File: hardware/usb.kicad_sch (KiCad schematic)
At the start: 24 parts, among them J3 USB_C_Receptacle, Q1 Q_NMOS_DGS, Q2 MBT2222ADW1T1, U10 CP2102N-Axx-xQFN24

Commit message: fixing submodule
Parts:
- removed Q1: Q_NMOS_DGS, Package_TO_SOT_SMD:SOT-323_SC-70, symbol Device:Q_NMOS_DGS
- removed R27, R60: 100k, Resistor_SMD:R_0402_1005Metric, symbol Device:R_Small
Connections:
- net CP2102N_~{SUS}: now reaches R29.1, U10.15 (~{SUSPEND})
- net CP2102N_RTS: now reaches Q2.4 (E2), R30.2, U10.19 (~{RTS})
- net CP2102N_DTR: now reaches Q2.1 (E1), R31.1, U10.23 (~{DTR})
- net USB_POWER_GOOD: now reaches U10.8 (VBUS)
- net DTR_BASE: now reaches Q2.5 (B2), R31.2
- net ~{RTS}_BASE: now reaches Q2.2 (B1), R30.1
- net 3V3_CORE renamed VDD_USB_3V3
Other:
- moved on the sheet: Q2A, Q2B, R30, R31

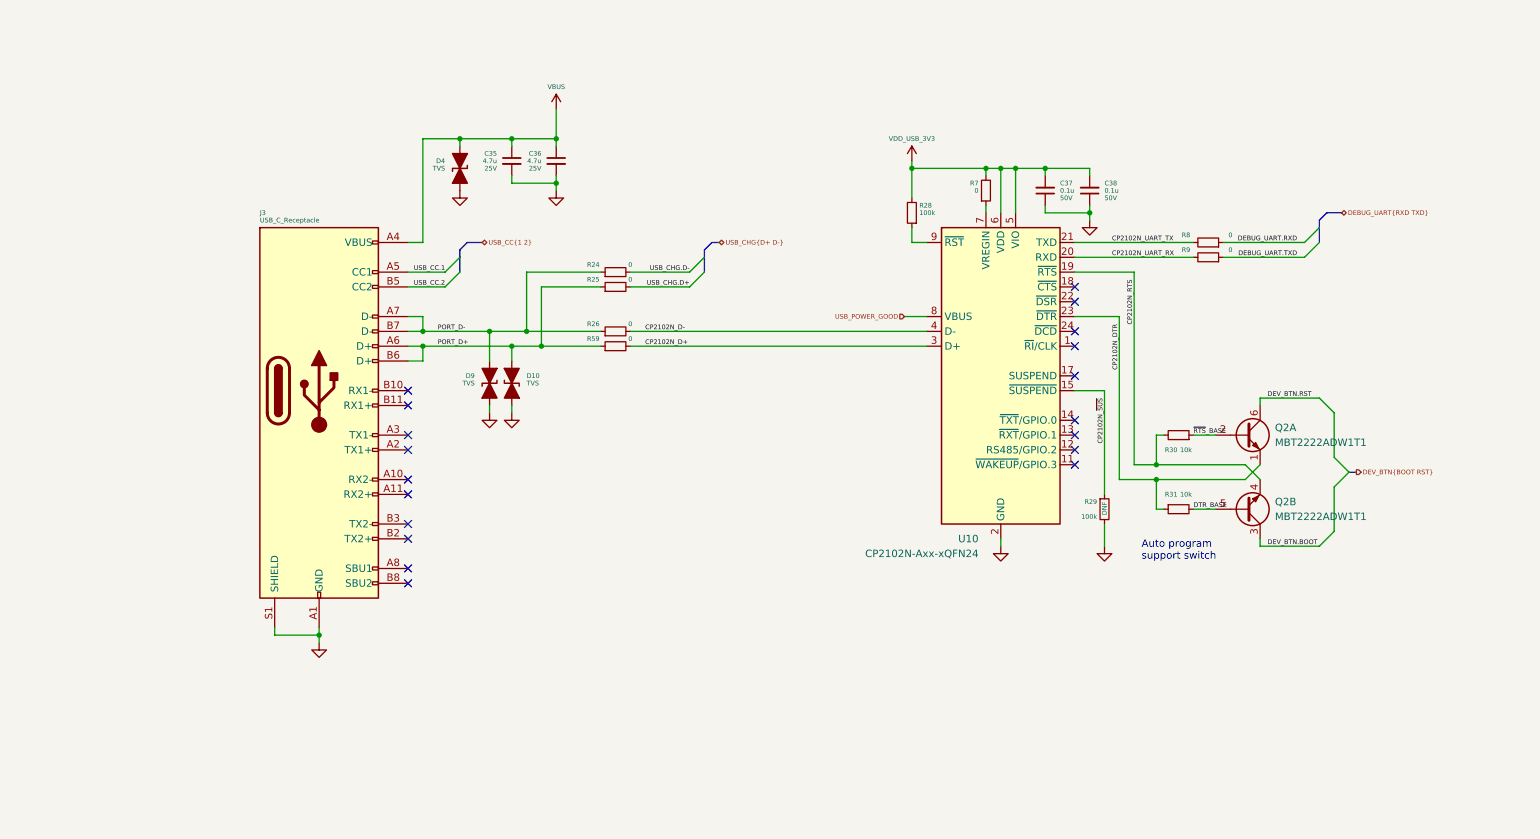
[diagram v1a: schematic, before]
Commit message: schematic tidy up, component placement, shielding investigation
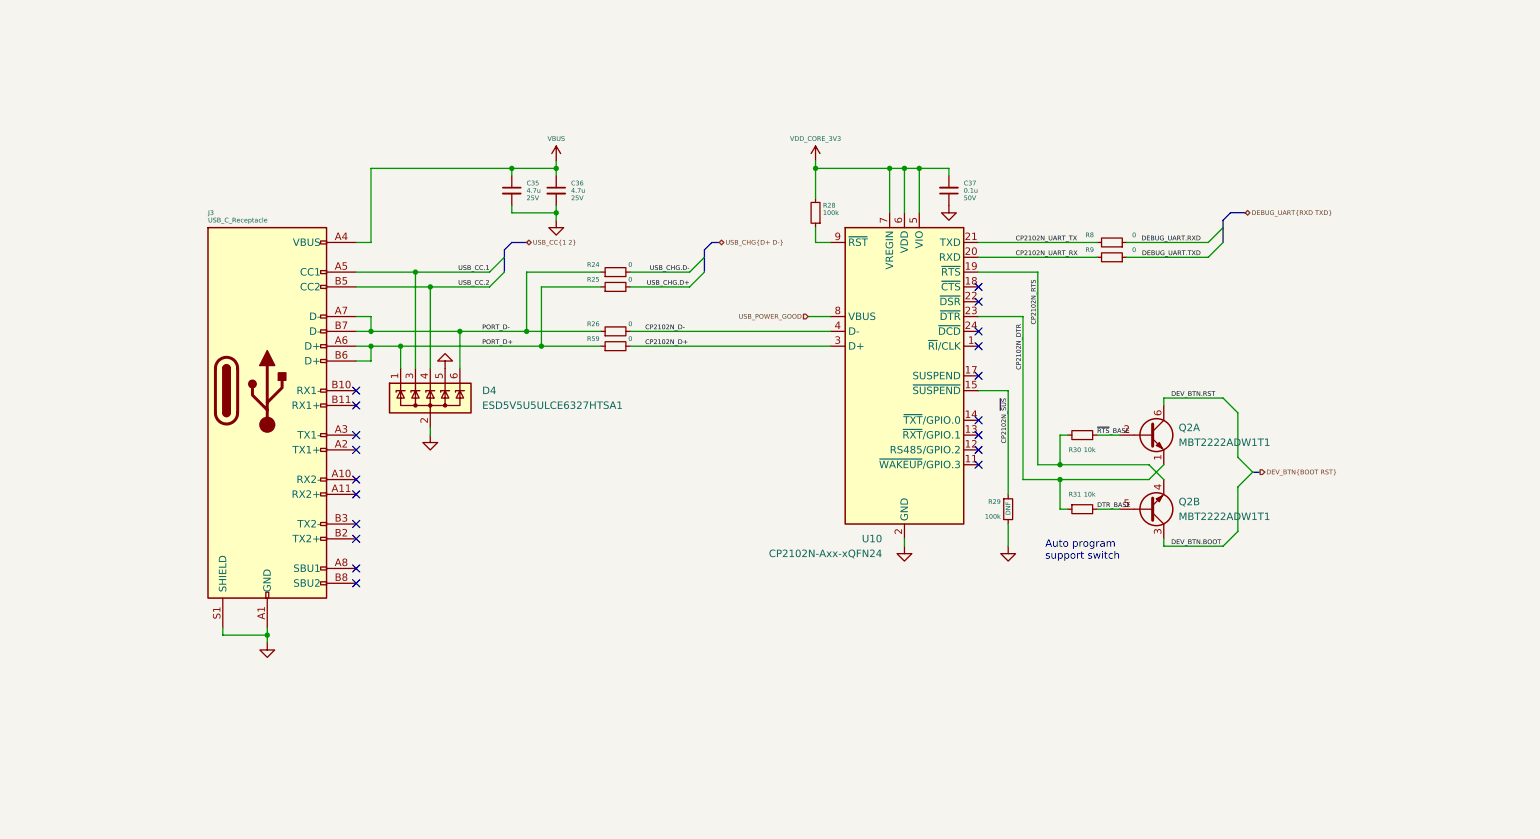
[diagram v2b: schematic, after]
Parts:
- removed C38: 0.1u, Capacitor_SMD:C_0402_1005Metric, symbol Device:C_Small
- removed D10, D4, D9: TVS, Diode_SMD:D_SOD-523, symbol Device:D_TVS_Filled
- removed R7: 0, Resistor_SMD:R_0402_1005Metric, symbol Device:R_Small
- added D4: ESD5V5U5ULCE6327HTSA1, Package_TO_SOT_SMD:SOT-363_SC-70-6, symbol Power_Protection:SP0505BAJT
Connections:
- net VDD_USB_3V3 is gone; now on net 3V3_CORE: C37.2, R28.2, U10.5 (VIO), U10.6 (VDD)
- net GND: now also D4.2 (A), D4.5 (K)
- net PORT_D+: now also D4.1 (K)
- net PORT_D-: now also D4.6 (K)
- net USB_CC.1: now also D4.3 (K)
- net USB_CC.2: now also D4.4 (K)
- net 3V3_CORE: now reaches U10.7 (VREGIN)
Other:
- moved on the sheet: C35, C36, C37, J3, Q2A, Q2B, R28, R29, R30, R31, R8, R9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

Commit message: minor sch tweaks, more layout, added power emc shield
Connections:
- net GND: no longer D4.5 (K)
- net 3V3_CORE renamed VDD_CORE_3V3
- no-connect marks 19 -> 20
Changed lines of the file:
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@@
   (no_connect (at 170.18 106.68))
   (no_connect (at 170.18 109.22))
+  (no_connect (at 78.74 97.79))
   (bus_entry (at 212.09 76.2) (size -2.54 2.54)
     (stroke (width 0) (type default) (color 0 0 0 0))
@@
     (effects (font (size 0.8 0.8)) (justify left))
   )
-  (symbol (lib_id "power:GND") (at 78.74 97.79 180) (unit 1)
-    (in_bom yes) (on_board yes)
-    (property "Reference" "#PWR0101" (id 0) (at 78.74 91.44 0)
-      (effects (font (size 0.8 0.8)) hide)
-    )
-    (property "Value" "GND" (id 1) (at 82.55 96.52 0)
-      (effects (font (size 0.8 0.8)) hide)
-    )
-    (property "Footprint" "" (id 2) (at 78.74 97.79 0)
-      (effects (font (size 0.8 0.8)) hide)
-    )
-    (property "Datasheet" "" (id 3) (at 78.74 97.79 0)
-      (effects (font (size 0.8 0.8)) hide)
-    )
-    (pin "1")
-  )
   (symbol (lib_id "power:GND") (at 76.2 109.22 0) (unit 1)

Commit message: screen mock, tweaked layout easier powerplane division
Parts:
- added C50: 4.7u, Capacitor_SMD:C_0603_1608Metric, symbol Device:C_Small
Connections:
- net GND: now also C50.2
- net VBUS: now also C50.1
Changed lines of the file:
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@@
   (junction (at 66.04 93.98) (diameter 0) (color 0 0 0 0)
   )
+  (junction (at 90.17 71.12) (diameter 0) (color 0 0 0 0)
+  )
   (junction (at 92.71 91.44) (diameter 0) (color 0 0 0 0)
   )
@@
   )
   (junction (at 154.94 63.5) (diameter 0) (color 0 0 0 0)
+  )
+  (junction (at 82.55 63.5) (diameter 0) (color 0 0 0 0)
   )
   (junction (at 97.79 71.12) (diameter 0) (color 0 0 0 0)
@@
     (stroke (width 0) (type default) (color 0 0 0 0))
   )
+  (wire (pts (xy 82.55 64.77) (xy 82.55 63.5))
+    (stroke (width 0) (type default) (color 0 0 0 0))
+  )
   (wire (pts (xy 201.93 102.87) (xy 212.09 102.87))
     (stroke (width 0) (type default) (color 0 0 0 0))
@@
     (stroke (width 0) (type default) (color 0 0 0 0))
   )
-  (wire (pts (xy 66.04 63.5) (xy 90.17 63.5))
+  (wire (pts (xy 66.04 63.5) (xy 82.55 63.5))
     (stroke (width 0) (type default) (color 0 0 0 0))
   )
@@
     (stroke (width 0) (type default) (color 0 0 0 0))
   )
+  (wire (pts (xy 82.55 69.85) (xy 82.55 71.12))
+    (stroke (width 0) (type default) (color 0 0 0 0))
+  )
   (wire (pts (xy 214.63 105.41) (xy 212.09 102.87))
     (stroke (width 0) (type default) (color 0 0 0 0))
@@
     (stroke (width 0) (type default) (color 0 0 0 0))
   )
+  (wire (pts (xy 82.55 71.12) (xy 90.17 71.12))
+    (stroke (width 0) (type default) (color 0 0 0 0))
+  )
   (bus (pts (xy 123.19 81.28) (xy 123.19 78.74))
     (stroke (width 0) (type default) (color 0 0 0 0))
@@
   )
   (wire (pts (xy 110.49 91.44) (xy 144.78 91.44))
+    (stroke (width 0) (type default) (color 0 0 0 0))
+  )
+  (wire (pts (xy 82.55 63.5) (xy 90.17 63.5))
     (stroke (width 0) (type default) (color 0 0 0 0))
   )
@@
       (effects (font (size 0.8 0.8)) (justify left))
     )
+    (pin "1")
+    (pin "2")
+  )
+  (symbol (lib_id "Device:C_Small") (at 82.55 67.31 0) (unit 1)
+    (in_bom yes) (on_board yes)
+    (property "Reference" "C50" (id 0) (at 85.09 66.04 0)
+      (effects (font (size 0.8 0.8)) (justify left))
+    )
+    (property "Value" "4.7u" (id 1) (at 85.09 67.31 0)
+      (effects (font (size 0.8 0.8)) (justify left))
+    )
+    (property "Footprint" "Capacitor_SMD:C_0603_1608Metric" (id 2) (at 82.55 67.31 0)
+      (effects (font (size 0.8 0.8)) hide)
+    )
+    (property "Datasheet" "~" (id 3) (at 82.55 67.31 0)
+      (effects (font (size 0.8 0.8)) hide)
+    )
+    (property "Voltage" "25V" (id 4) (at 85.09 68.58 0)
+      (effects (font (size 0.8 0.8)) (justify left))
+    )

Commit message: Updates
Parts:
- removed C37: 0.1u, Capacitor_SMD:C_0402_1005Metric, symbol Device:C_Small
- removed C50: 4.7u, Capacitor_SMD:C_0603_1608Metric, symbol Device:C_Small
- removed J3: USB_C_Receptacle, bt_Connector_USB:AMPHENOL_124019032112A, symbol Connector:USB_C_Receptacle
- removed Q2: MBT2222ADW1T1, Package_TO_SOT_SMD:SOT-363_SC-70-6, symbol Transistor_BJT:MBT2222ADW1T1
- removed R28, R29: 100k, Resistor_SMD:R_0402_1005Metric, symbol Device:R_Small
- removed R30, R31: 10k, Resistor_SMD:R_0402_1005Metric, symbol Device:R_Small
- removed R8, R9: 0, Resistor_SMD:R_0402_1005Metric, symbol Device:R_Small
- removed U10: CP2102N-Axx-xQFN24, Package_DFN_QFN:QFN-24-1EP_4x4mm_P0.5mm_EP2.6x2.6mm, symbol Interface_USB:CP2102N-Axx-xQFN24
- added C? (x2): 4.7u, Capacitor_SMD:C_0603_1608Metric, symbol Device:C_Small
- added C?: 10p, Capacitor_SMD:C_0402_1005Metric, symbol Device:C_Small
- added C? (x7): 10u, Capacitor_SMD:C_0603_1608Metric, symbol Device:C_Small
- added C? (x2): 0.1u, Capacitor_SMD:C_0402_1005Metric, symbol Device:C_Small
- added C?: 1u, Capacitor_SMD:C_0402_1005Metric, symbol Device:C_Small
- added D?: MBR0540, LED_SMD:LED_0603_1608Metric, symbol Device:D_Zener_Small_Filled
- added D?: LED_Small_Filled, LED_SMD:LED_0402_1005Metric, symbol Device:LED_Small_Filled
- added J?: USB_C_Receptacle_USB2.0, symbol Connector:USB_C_Receptacle_USB2.0
- added J?: BATTERY, symbol Connector:Conn_01x03_Male
- added L?: 1u, Inductor_SMD:L_Wuerth_MAPI-2510, symbol Device:L_Small
- added L?: 0.47u, Inductor_SMD:L_Wuerth_MAPI-2510, symbol Device:L_Small
- added R? (x4): 0, Resistor_SMD:R_0402_1005Metric, symbol Device:R_Small
- added R? (x3): 14k, Resistor_SMD:R_0402_1005Metric, symbol Device:R_Small
- added R? (x3): 100k, Resistor_SMD:R_0402_1005Metric, symbol Device:R_Small
- added R? (x2): 1k, Resistor_SMD:R_0402_1005Metric, symbol Device:R_Small
- added R?: ?, Resistor_SMD:R_0402_1005Metric, symbol Device:R_Small
- added SW?: SW_Push, symbol Switch:SW_Push
- added U?: MP2723, bt_Package_QFN:MP_QFN-26-3.5x3.5_P0.45mm, symbol bt_PMIC_Battery_Charger:MP2723
- added U?: TLV62569DBV, Package_TO_SOT_SMD:SOT-23-5, symbol Regulator_Switching:TLV62569DBV
- added U?: MAX17048G, Package_DFN_QFN:TDFN-8-1EP_2x2mm_P0.5mm_EP0.8x1.2mm, symbol bt_PMIC_Battery_Management:MAX17048G
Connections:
- net GND: now also C?.2, C?.2, C?.2, C?.2, C?.2, C?.2, C?.2, C?.2, C?.2, C?.2, C?.2, J?.3 (Pin_3), J?.A1 (GND), J?.A12 (GND), J?.B1 (GND), J?.B12 (GND), J?.S1 (SHIELD), R?.2, R?.2, R?.2, R?.2, R?.2, R?.2, U?.1 (CTG), U?.15 (AGND), U?.2 (GND), U?.4 (GND), U?.5 (PGND), U?.6 (QSTRT), U?.6-7 (PGND)
- net PORT_D+: now also J?.A6 (D+), J?.B6 (D+)
- net PORT_D-: now also J?.A7 (D-), J?.B7 (D-)
- net USB_CHG.D+: now also U?.1-26 (DP)
- net USB_CHG.D-: now also U?.25 (DM)
- net VBUS: now also C?.1, J?.A4 (VBUS), J?.A9 (VBUS), J?.B4 (VBUS), J?.B9 (VBUS), U?.2 (IN)
- net CP2102N_D+ renamed USB_ESP.D+
- net CP2102N_D- renamed USB_ESP.D-
- net USB_CC.1: no longer names the net of D4.3 (K)
- net USB_CC.2: no longer names the net of D4.4 (K)
- new net: L?.1, U?.3 (SW)
- new net: C?.2, R?.1, R?.2, U?.5 (FB)
- new net: J?.B5 (CC2), R?.1
- new net: R?.1, U?.12 (VNTC)
- new net: R?.2, R?.2, U?.11 (NTC)
- new net: R?.1, U?.24 (ILIM)
- new net: R?.1, U?.23 (OTG)
- new net: J?.A5 (CC1), R?.1
- new net: J?.2 (Pin_2), R?.1
- new net: D?.2 (A), R?.2
- new net: R?.1, U?.18 (~{CE})
- new net: R?.2, U?.22 (DISC)
- new net: C?.1, U?.3 (PMID)
- new net: C?.2, L?.1, U?.4 (SW)
- new net: C?.1, U?.8 (BST)
- new net: D?.1 (K), U?.9 (STAT)
- new net: R?.1, SW?.1
- new net +3V3: C?.1, C?.1, C?.1, L?.2, R?.1, R?.2
- new net +BATT: C?.1, C?.1, J?.1 (Pin_1), U?.17 (BATT), U?.2 (CELL), U?.3 (VDD)
- new net BMS_INT: U?.10 (INT), U?.5 (~{ALRT})
- new net BOOTSTRAP: D?.2 (A), SW?.2
- new net POWER_EN: D?.1 (K), R?.1, U?.1 (EN)
- new net SENSOR_I2C.SCL: U?.19-20 (SCL), U?.7 (SCL)
- new net SENSOR_I2C.SDA: U?.21 (SDA), U?.8 (SDA)
- new net VDD_NVDC: C?.1, C?.1, C?.1, C?.1, L?.2, U?.16 (SYS), U?.4 (VIN)
- new net VREF: C?.1, R?.1, R?.1, U?.13-14 (VREF)
- no-connect marks 20 -> 2
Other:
- note added: "0x6C/0x6D"
- note added: "Bootstrap allows hard shutdown of core rail, startup via button or other source. Shutdown triggered by ESP pulling low."
- note added: "Button Control"
- note added: "MCU Control"
- note added: "TODO: Get 3V from NVDC"
- note removed: "Auto program support switch"
- moved on the sheet: C35, C36, D4, R24, R25, R26, R59

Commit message: changing sdmmc to spi to support lcd rgb mode
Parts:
- added R?: 0, Resistor_SMD:R_0402_1005Metric, symbol Device:R_Small
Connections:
- net POWER_EN: now also R?.1; no longer D?.1 (K), R?.1, U?.1 (EN)
- net VDD_NVDC: now also R?.2
- new net: D?.1 (K), R?.1, R?.2, U?.1 (EN)
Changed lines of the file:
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@@
+    (stroke (width 0) (type default) (color 0 0 0 0))
+  )
+  (wire (pts (xy 64.77 142.24) (xy 71.12 142.24))
     (stroke (width 0) (type default) (color 0 0 0 0))
   )
@@
     (stroke (width 0) (type default) (color 0 0 0 0))
   )
+  (wire (pts (xy 46.99 142.24) (xy 59.69 142.24))
+    (stroke (width 0) (type default) (color 0 0 0 0))
+  )
+  (wire (pts (xy 48.26 120.65) (xy 48.26 118.11))
+    (stroke (width 0) (type default) (color 0 0 0 0))
+  )
   (wire (pts (xy 60.96 74.93) (xy 76.2 74.93))
     (stroke (width 0) (type default) (color 0 0 0 0))
@@
   )
   (wire (pts (xy 142.24 62.23) (xy 142.24 63.5))
-    (stroke (width 0) (type default) (color 0 0 0 0))
-  )
-  (wire (pts (xy 46.99 142.24) (xy 71.12 142.24))
     (stroke (width 0) (type default) (color 0 0 0 0))
   )
@@
   (label "VREF" (at 218.44 52.07 180)
     (effects (font (size 0.8 0.8) (thickness 0.16) bold) (justify right bottom))
-  )
-  (label "POWER_EN" (at 59.69 142.24 0)
-    (effects (font (size 0.8 0.8)) (justify left bottom))
   )
   (label "PORT_D+" (at 80.01 77.47 0)
@@
       (effects (font (size 0.8 0.8)) hide)
     )
+    (pin "1")
+    (pin "2")
+  )
+  (symbol (lib_id "Device:R_Small") (at 62.23 142.24 90) (unit 1)
+    (in_bom yes) (on_board yes)
+    (property "Reference" "R?" (id 0) (at 59.69 140.97 90)
+      (effects (font (size 0.8 0.8)) (justify left))
+    )
+    (property "Value" "0" (id 1) (at 67.31 140.97 90)
+      (effects (font (size 0.8 0.8)) (justify left))
+    )
+    (property "Footprint" "Resistor_SMD:R_0402_1005Metric" (id 2) (at 62.23 142.24 0)
+      (effects (font (size 0.8 0.8)) hide)
+    )
+    (property "Datasheet" "~" (id 3) (at 62.23 142.24 0)
+      (effects (font (size 0.8 0.8)) hide)
+    )
